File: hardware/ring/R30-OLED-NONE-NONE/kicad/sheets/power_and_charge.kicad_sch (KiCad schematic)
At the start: 17 parts, among them Q1 SI2301, Q2 2N7002, U3 TP4054, U4 RT9080-33GJ5

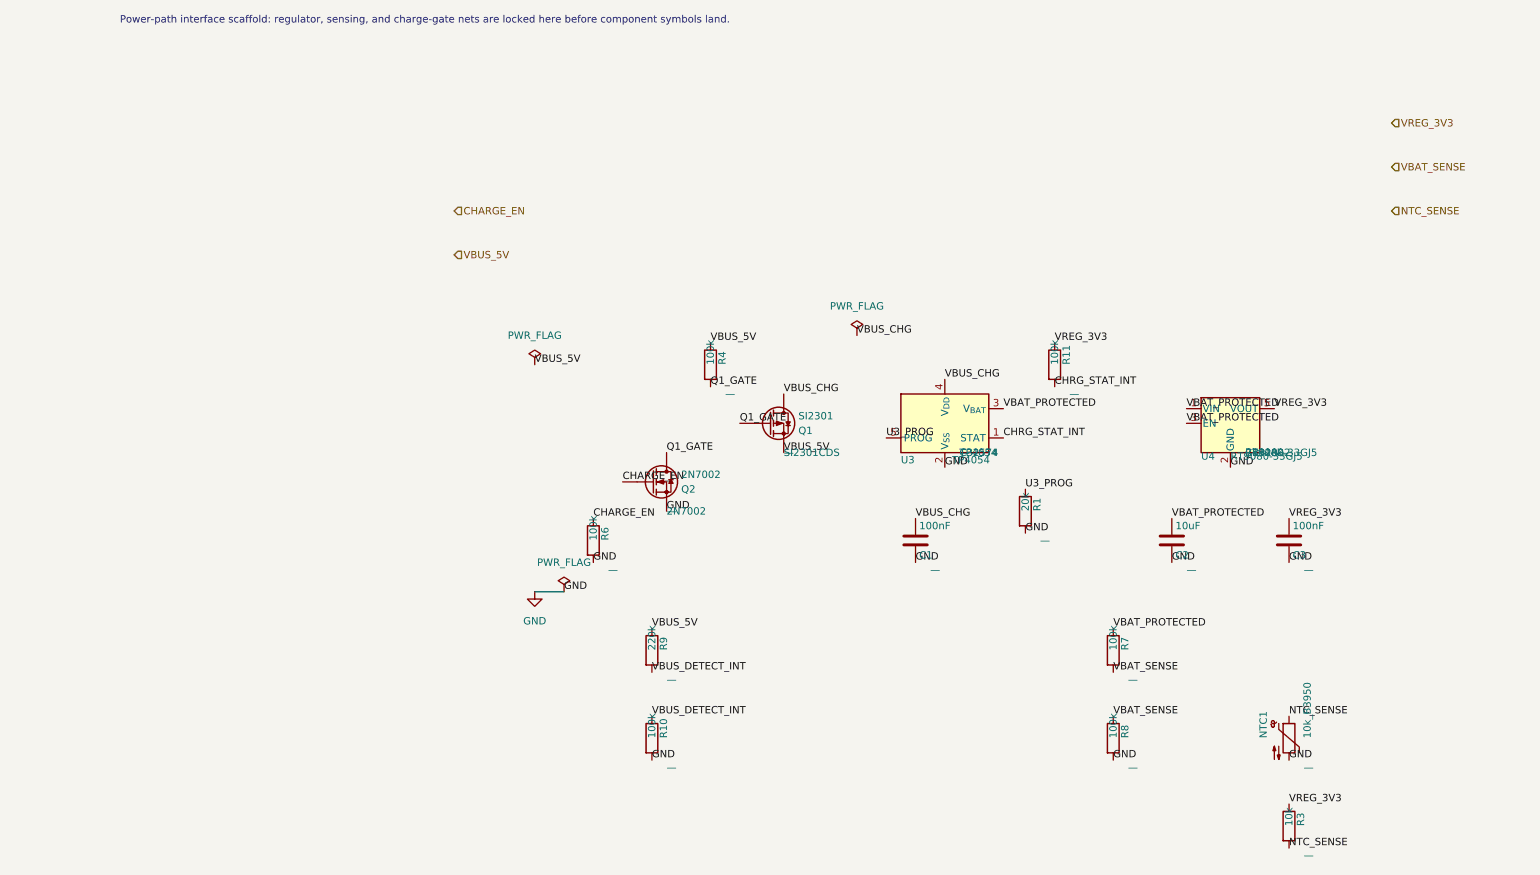
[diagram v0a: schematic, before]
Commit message: feat(hardware): lock R30 sense and schematic baseline
Design disclosure: sensing mechanism PAW3204-class optical tracking; form factor R30-OLED-NONE-NONE fingertip ring, active 30-degree ring packet; intended use BLE HID pointing for accessibility; BOM estimate ~$5.30-9.45.

Record the accepted 2N7002 charge-gate path, R7-R11 sense/status values, current KiCad red baseline, and directly linked packet truth docs.
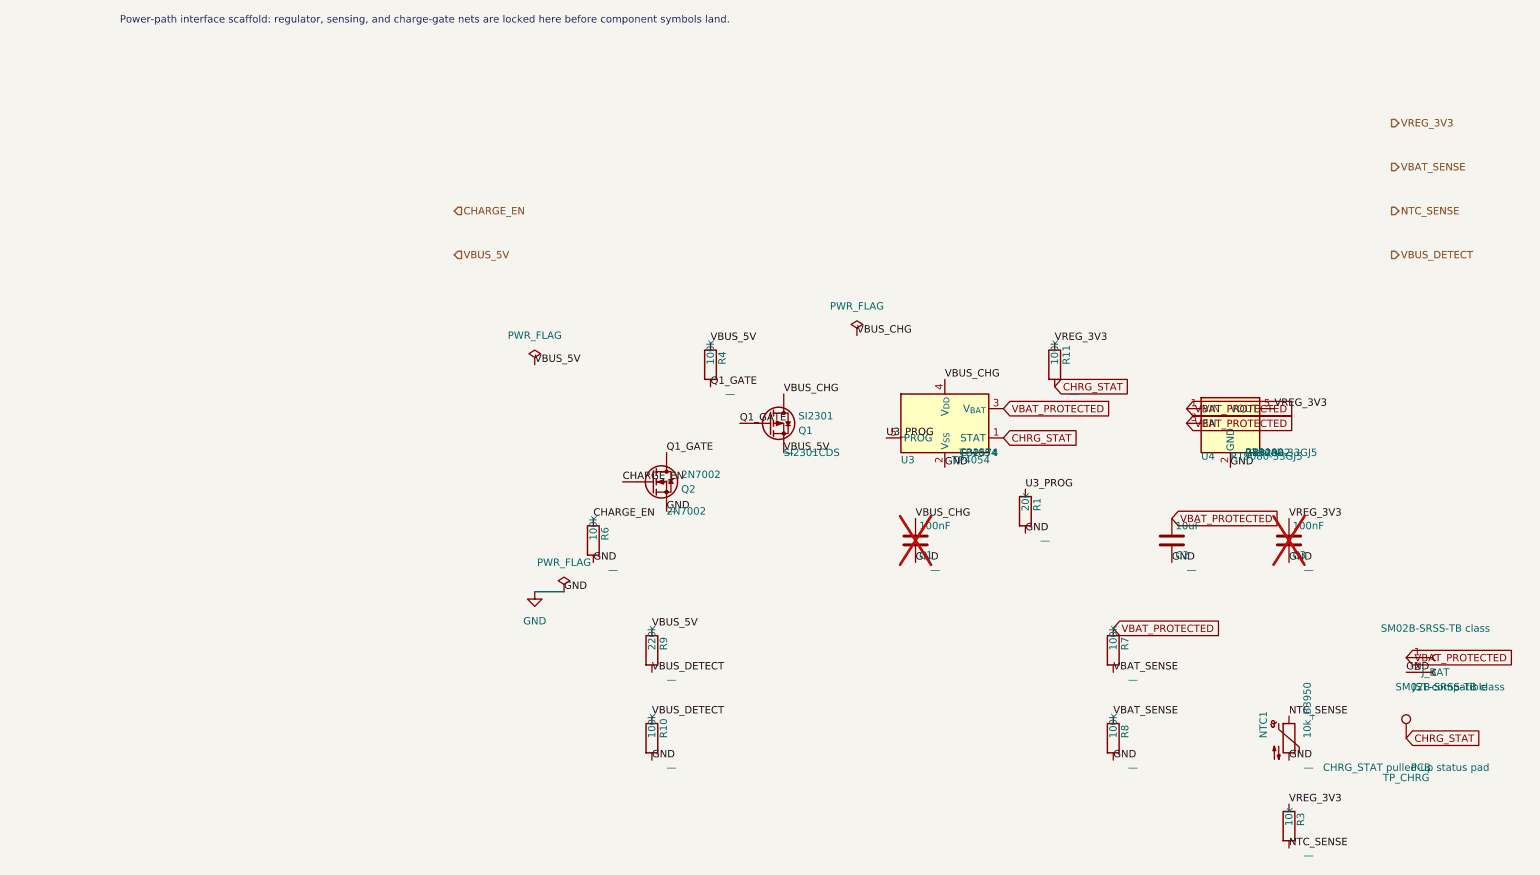
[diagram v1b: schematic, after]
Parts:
- added J_BAT: SM02B-SRSS-TB class, PowerFinger_Ring:JST_SH_SM02B-SRSS-TB_RA_1x02_P1.00mm, symbol Connector:Conn_01x02_Socket
- added TP_CHRG: CHRG_STAT pulled-up status pad, TestPoint:TestPoint_Pad_D1.0mm, symbol Connector:TestPoint
- C1, C3: now not fitted; now left out of the parts list
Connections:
- net GND: now also J_BAT.2 (Pin_2)
- net VBAT_PROTECTED: now also J_BAT.1 (Pin_1)
- net CHRG_STAT_INT renamed CHRG_STAT
- net CHRG_STAT: now also TP_CHRG.1
- net VBUS_DETECT_INT renamed VBUS_DETECT
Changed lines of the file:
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@@
 		(unit 1)
 		(exclude_from_sim no)
-		(in_bom yes)
-		(on_board yes)
-		(dnp no)
+		(in_bom no)
+		(on_board no)
+		(dnp yes)
 		(fields_autoplaced no)
 		(property "Reference" "C1"
@@
 		(unit 1)
 		(exclude_from_sim no)
-		(in_bom yes)
-		(on_board yes)
-		(dnp no)
+		(in_bom no)
+		(on_board no)
+		(dnp yes)
 		(fields_autoplaced no)
 		(property "Reference" "C3"
@@
 		)
 	)
+	(symbol
+		(lib_id "Connector:Conn_01x02_Socket")
+		(at 195.58 130.81 0)
+		(unit 1)
+		(exclude_from_sim no)
+		(in_bom yes)
+		(on_board yes)
+		(dnp no)
+		(fields_autoplaced no)
+		(property "Reference" "J_BAT"
+			(at 195.58 133.35 0)
+			(effects
+				(font
+					(size 1.27 1.27)
+				)
+			)
+		)
+		(property "Value" "SM02B-SRSS-TB class"
+			(at 195.58 125.73 0)
+			(effects
+				(font
+					(size 1.27 1.27)
+				)
+			)
+		)
+		(property "Footprint" "PowerFinger_Ring:JST_SH_SM02B-SRSS-TB_RA_1x02_P1.00mm"
+			(at 195.58 130.81 0)
+			(effects
+				(font
+					(size 1.27 1.27)
+				)
+				(hide yes)
+			)
+		)
+		(property "mfg_part_num" "SM02B-SRSS-TB class"
+			(at 198.12 135.8899 0)
+			(effects
+				(font
+					(size 1.27 1.27)
+				)
+			)
+		)
+		(property "manufacturer" "JST-compatible"
+			(at 198.12 135.8899 0)
+			(effects
+				(font
+					(size 1.27 1.27)
+				)
+			)
+		)
+		(property "lcsc" ""
+			(at 198.12 135.8899 0)
+			(effects
+				(font
+					(size 1.27 1.27)
+				)
+			)
+		)
+		(pin "1"
+		)
+		(pin "2"
+		)
+		(instances
+			(project "simple_circuit"
+				(path "/3bb73a68-f2e3-4fdc-8035-844d8d9ecf61"
+					(reference "J_BAT")
+					(unit 1)
+				)
+			)
+		)
+	)
+	(symbol
+		(lib_id "Connector:TestPoint")
+		(at 190.5 144.78 0)
+		(unit 1)
+		(exclude_from_sim no)
+		(in_bom yes)
+		(on_board yes)
+		(dnp no)
+		(fields_autoplaced no)
+		(property "Reference" "TP_CHRG"
+			(at 190.5 151.638 0)
+			(effects
+				(font
+					(size 1.27 1.27)
+				)
+			)
+		)
+		(property "Value" "CHRG_STAT pulled-up status pad"
+			(at 190.5 149.86 0)
+			(effects
+				(font
+					(size 1.27 1.27)
+				)
+			)
+		)
+		(property "Footprint" "TestPoint:TestPoint_Pad_D1.0mm"
+			(at 195.58 144.78 0)
+			(effects
+				(font
+					(size 1.27 1.27)
+				)
+				(hide yes)
+			)
+		)
+		(property "mfg_part_num" ""
+			(at 193.04 149.8599 0)
+			(effects
+				(font
+					(size 1.27 1.27)
+				)
+			)
+		)
+		(property "manufacturer" "PCB"
+			(at 193.04 149.8599 0)
+			(effects
+				(font
+					(size 1.27 1.27)
+				)
+			)
+		)
+		(property "lcsc" ""
+			(at 193.04 149.8599 0)
+			(effects
+				(font
+					(size 1.27 1.27)
+				)
+			)
+		)
+		(pin "1"
+		)
+		(instances
+			(project "simple_circuit"
+				(path "/3bb73a68-f2e3-4fdc-8035-844d8d9ecf61"
+					(reference "TP_CHRG")
+					(unit 1)
+				)
+			)
+		)
+	)
 	(wire
 		(pts
@@
 		)
 	)
-	(label "CHRG_STAT_INT"
+	(global_label "CHRG_STAT"
+		(shape input)
 		(at 120.65 92.71 0.0000)
 		(effects
@@
 		)
 	)
-	(label "VBAT_PROTECTED"
+	(global_label "VBAT_PROTECTED"
+		(shape input)
 		(at 120.65 87.63 0.0000)
 		(effects
@@
 		)
 	)
-	(label "CHRG_STAT_INT"
+	(global_label "CHRG_STAT"
+		(shape input)
 		(at 129.54 83.82 0.0000)
 		(effects
@@
 		)
 	)
-	(label "VBAT_PROTECTED"
+	(global_label "VBAT_PROTECTED"
+		(shape input)
 		(at 152.4 87.63 0.0000)
 		(effects
@@
 		)
 	)
-	(label "VBAT_PROTECTED"
+	(global_label "VBAT_PROTECTED"
+		(shape input)
 		(at 152.4 90.17 0.0000)
 		(effects
@@
 		)
 	)
-	(label "VBAT_PROTECTED"
+	(global_label "VBAT_PROTECTED"
+		(shape input)
 		(at 149.86 106.68 0.0000)
 		(effects
@@
 		)
 	)
-	(label "VBAT_PROTECTED"
+	(global_label "VBAT_PROTECTED"
+		(shape input)
 		(at 139.7 125.73 0.0000)
 		(effects
@@
 		)
 	)
-	(label "VBUS_DETECT_INT"
+	(label "VBUS_DETECT"
 		(at 59.69 133.35 0.0000)
 		(effects
@@
 		)
 	)
-	(label "VBUS_DETECT_INT"
+	(label "VBUS_DETECT"
 		(at 59.69 140.97 0.0000)
 		(effects
@@
 		)
 	)
+	(global_label "VBAT_PROTECTED"
+		(shape input)
+		(at 190.5 130.81 0)
+		(effects
+			(font
+				(size 1.27 1.27)
+			)
+			(justify left bottom)
+		)
+	)
+	(label "GND"
+		(at 190.5 133.35 0)
+		(effects
+			(font
+				(size 1.27 1.27)
+			)
+			(justify left bottom)
+		)
+	)
+	(global_label "CHRG_STAT"
+		(shape input)
+		(at 190.5 144.78 0)
+		(effects
+			(font
+				(size 1.27 1.27)
+			)
+			(justify left bottom)
+		)
+	)
 	(hierarchical_label "VREG_3V3"
-		(shape input)
+		(shape output)
 		(at 187.96 38.1 180)
 		(effects
@@
 	)
 	(hierarchical_label "VBAT_SENSE"
-		(shape input)
+		(shape output)
 		(at 187.96 45.72 180)
 		(effects
@@
 	)
 	(hierarchical_label "NTC_SENSE"
-		(shape input)
+		(shape output)
 		(at 187.96 53.34 180)
 		(effects
@@
 		(effects
 			(font
+				(size 1.27 1.27)
+			)
+			(justify left)
+		)
+	)
+	(hierarchical_label "VBUS_DETECT"
+		(shape output)
+		(at 187.96 60.96 180)
+		(effects
+			(font

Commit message: fix(r30): clean schematic erc library baseline
Design disclosure: sensing mechanism PAW3204-class optical tracking; form factor R30-OLED-NONE-NONE fingertip ring, active 30-degree ring packet; intended use BLE HID pointing for accessibility; BOM estimate ~$5.30-9.45.

Materialize the project-local PowerFinger symbol and PowerFinger_Ring footprint libraries, wire sheet-interface labels, keep PAW3204 reset/motion local to sensor test pads, and update the verified KiCad snapshot to ERC=0, DRC=349, unconnected=41, parity=118.
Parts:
- NTC1: footprint Resistor_SMD:R_0402_1005Metric -> PowerFinger_Ring:Thermistor_NTC_0402_1005Metric
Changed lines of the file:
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@@
 			)
 		)
-		(property "Footprint" "Resistor_SMD:R_0402_1005Metric"
+		(property "Footprint" "PowerFinger_Ring:Thermistor_NTC_0402_1005Metric"
 			(at 170.18 146.05 0.0000)
 			(effects
@@
 		)
 	)
+	(wire
+		(pts
+			(xy 25.4 53.34) (xy 33.02 53.34)
+		)
+		(stroke (width 0) (type default) (color 0 0 0 0))
+	)
+	(label "CHARGE_EN"
+		(at 33.02 53.34 0)
+		(effects
+			(font
+				(size 1.27 1.27)
+			)
+		)
+	)
+	(wire
+		(pts
+			(xy 25.4 60.96) (xy 33.02 60.96)
+		)
+		(stroke (width 0) (type default) (color 0 0 0 0))
+	)
+	(label "VBUS_5V"
+		(at 33.02 60.96 0)
+		(effects
+			(font
+				(size 1.27 1.27)
+			)
+		)
+	)
+	(wire
+		(pts
+			(xy 180.34 38.1) (xy 187.96 38.1)
+		)
+		(stroke (width 0) (type default) (color 0 0 0 0))
+	)
+	(label "VREG_3V3"
+		(at 180.34 38.1 180)
+		(effects
+			(font
+				(size 1.27 1.27)
+			)
+		)
+	)
+	(wire
+		(pts
+			(xy 180.34 45.72) (xy 187.96 45.72)
+		)
+		(stroke (width 0) (type default) (color 0 0 0 0))
+	)
+	(label "VBAT_SENSE"
+		(at 180.34 45.72 180)
+		(effects
+			(font
+				(size 1.27 1.27)
+			)
+		)
+	)
+	(wire
+		(pts
+			(xy 180.34 53.34) (xy 187.96 53.34)
+		)
+		(stroke (width 0) (type default) (color 0 0 0 0))
+	)
+	(label "NTC_SENSE"
+		(at 180.34 53.34 180)
+		(effects
+			(font
+				(size 1.27 1.27)
+			)
+		)
+	)
+	(wire
+		(pts
+			(xy 180.34 60.96) (xy 187.96 60.96)
+		)
+		(stroke (width 0) (type default) (color 0 0 0 0))
+	)
+	(label "VBUS_DETECT"
+		(at 180.34 60.96 180)
+		(effects
+			(font
+				(size 1.27 1.27)
+			)
+		)
+	)

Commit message: fix(r30): reduce pcb schematic parity
Sensing mechanism: PAW3204 optical surface tracking.\nForm factor and angle: R30 30-degree ring, OLED/NONE/NONE active lane.\nIntended use: accessibility-first BLE HID pointing first-board validation.\nBOM estimate: active R30 prototype remains about .30-.45, target about .
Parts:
- C2: footprint Capacitor_SMD:C_0402_1005Metric -> Capacitor_SMD:C_0603_1608Metric
- NTC1: value 10k_B3950 -> 10k B3950
- Q1: value SI2301 -> SI2301 P-FET
- Q2: value 2N7002 -> 2N7002 gate driver
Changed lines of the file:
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@@
 			)
 		)
-		(property "Value" "SI2301"
+		(property "Value" "SI2301 P-FET"
 			(at 85.09 88.9 0.0000)
 			(effects
@@
 			)
 		)
-		(property "Value" "2N7002"
+		(property "Value" "2N7002 gate driver"
 			(at 64.77 99.06 0.0000)
 			(effects
@@
 			)
 		)
-		(property "Footprint" "Capacitor_SMD:C_0402_1005Metric"
+		(property "Footprint" "Capacitor_SMD:C_0603_1608Metric"
 			(at 150.8252 106.68 0.0000)
 			(effects
@@
 			)
 		)
-		(property "Value" "10k_B3950"
+		(property "Value" "10k B3950"
 			(at 173.355 144.78 90)
 			(effects
